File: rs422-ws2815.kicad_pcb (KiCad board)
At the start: 2 copper layers, 94 x 18.5 mm, 32 parts, among them J1 12V, J10 DO, J11 DI, J12 GND, J13 +5V OUT, J2 12V, J3 12V, J4 A, J5 B, J6 GND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

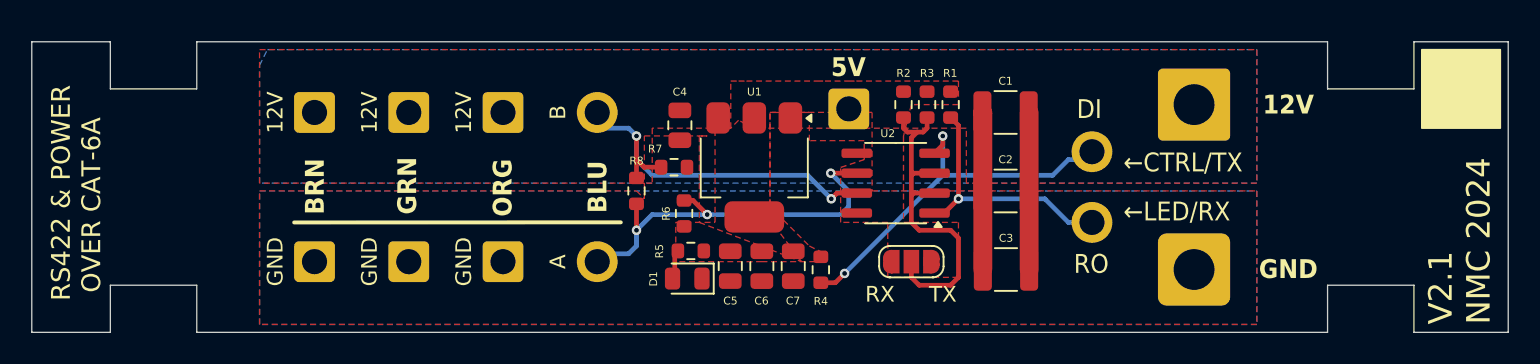
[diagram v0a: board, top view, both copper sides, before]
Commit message: Add files via upload
Changed to TI TLV761 5V reg & updated caps to suit
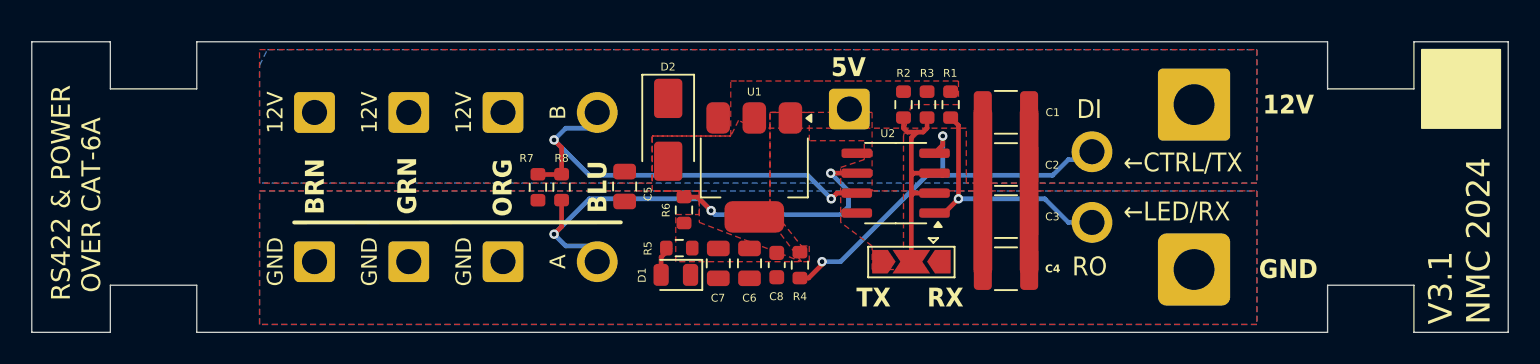
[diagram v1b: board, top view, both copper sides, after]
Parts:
- added C4: EMK325ABJ107MM-T, Capacitor_SMD:C_1210_3225Metric, F.Cu at (107.5, 73.5)
- added D2: 1N4002 M2, Diode_SMD:D_SMA, F.Cu at (86.0, 64.6)
- C5: renamed from C4; value 10uF -> 1uF Tantalum
- C6: renamed from C5; value 22uF -> 2.2uF
- C8: renamed from C7; footprint Capacitor_SMD:C_0805_2012Metric -> Capacitor_SMD:C_0603_1608Metric
- D1: value LED -> LED KT-0805B
- JP1: value SolderJumper -> TX/RX Jumper; footprint Jumper:SolderJumper-3_P1.3mm_Open_RoundedPad1.0x1.5mm_NumberLabels -> Jumper:SolderJumper-3_P2.0mm_Open_TrianglePad1.0x1.5mm
- U1: value AMS1117-5.0 -> TLV76150DCYR
- moved R7 8.76 mm to (77.7, 68.3), turned to -90 degrees
- moved C5 5.25 mm to (83.2, 68.2)
- moved R8 4.78 mm to (79.2, 68.3)
- moved C3 3.37 mm to (107.5, 70.1)
- moved C7 2.78 mm to (89.2, 73.1)
- moved C2 1.68 mm to (107.5, 66.8)
- moved R4 1.36 mm to (94.4, 73.2)
- moved C6 1.24 mm to (91.2, 73.1)
- moved C8 1.05 mm to (92.9, 73.2)
- moved D1 0.76 mm to (86.5, 73.8)
- moved R5 0.76 mm to (86.7, 72.1)
- moved R6 0.22 mm to (87.0, 69.7)
- turned JP1 to 180 degrees
- renumbered C6 to C7
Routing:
- net Net-(JP1-C): track 22.4 -> 14.5 mm
- net /A: track 25.6 -> 31.6 mm
- net /B: track 23.9 -> 27.7 mm
- net /DI FROM CTRL: track 24.3 -> 25.8 mm
- net Net-(D1-A): track 2.51 -> 1.94 mm
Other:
- board text added: "RX"
- board text added: "TX"
- board text added: "V3.1 NMC 2024"
- board text removed: "V2.1 NMC 2024"
